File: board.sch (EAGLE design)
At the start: 31 parts, among them U3 STM32F405RG

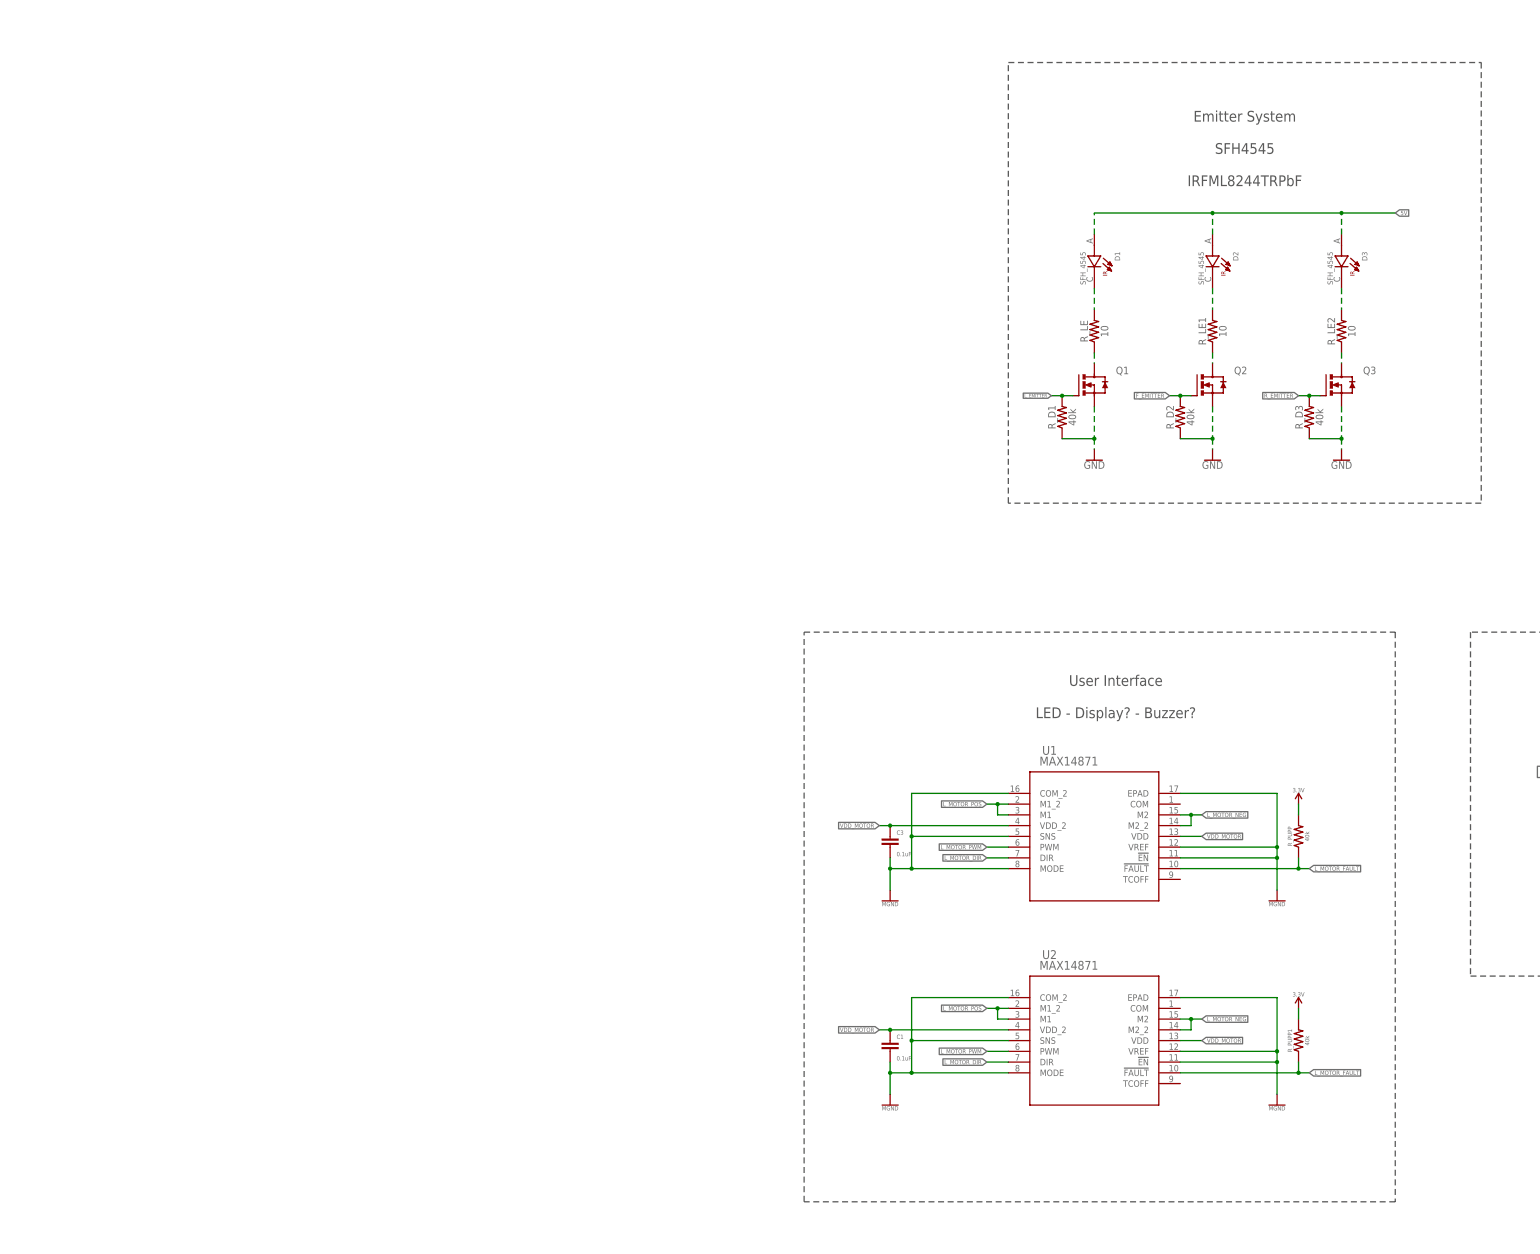
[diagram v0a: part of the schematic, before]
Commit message: Update Motor driver -> MAX14870
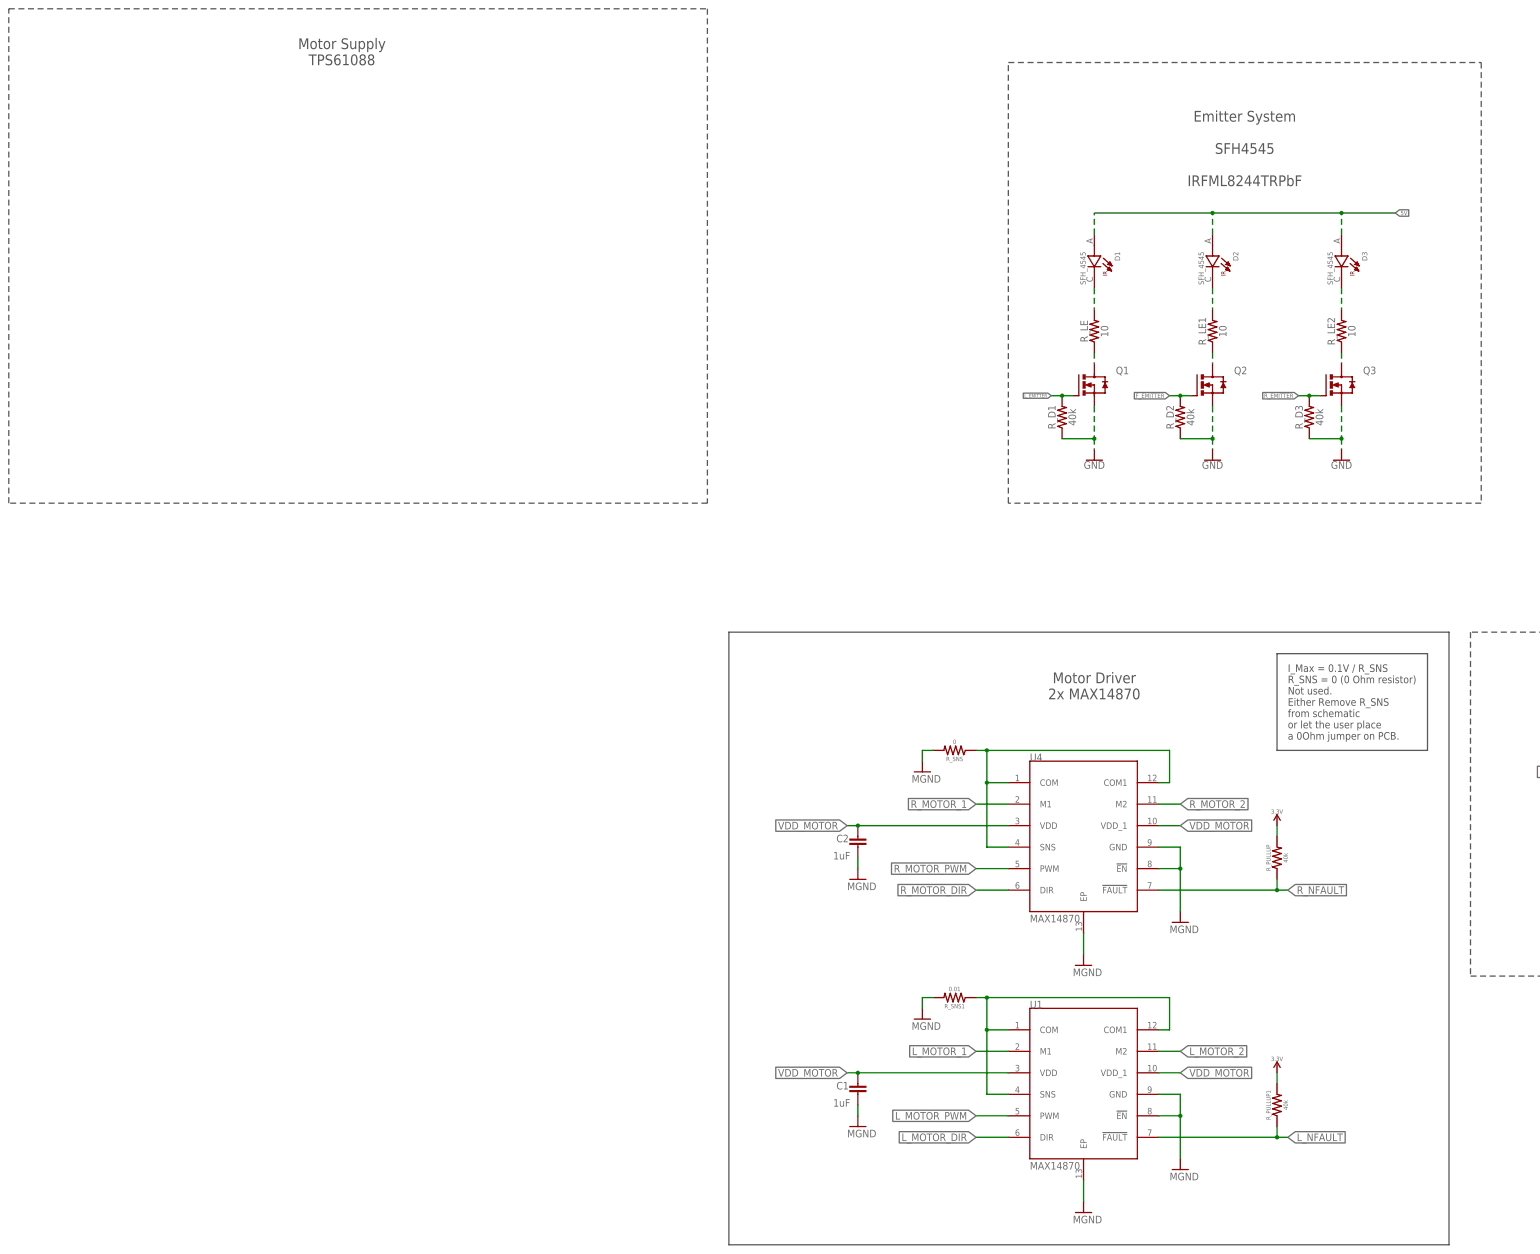
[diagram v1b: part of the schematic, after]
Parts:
- removed C3: 0.1uF, SparkFun-Capacitors:0.1UF-0603-25V-5%
- removed R_PUPP, R_PUPP1: 40k, SparkFun-Resistors:2.2KOHM-0603-1/10W-1%
- removed U2: (no value), Isaks Bibliotek:MAX14871EUE
- added C2: 1uF, Resistor_Capacitor:CC0603JRNPO9BN220
- added R_PULLUP, R_PULLUP1: 40k, SparkFun-Resistors:2.2KOHM-0603-1/10W-1%
- added R_SNS: 0, SparkFun-Resistors:2.2KOHM-0603-1/10W-1%
- added R_SNS1: 0.01, SparkFun-Resistors:2.2KOHM-0603-1/10W-1%
- added U4: MAX14870, Isaks Bibliotek:MAX14870
- C1: value 0.1uF -> 1uF; device SparkFun-Capacitors:0.1UF-0603-25V-5% -> Resistor_Capacitor:CC0603JRNPO9BN220
- U1: value (none) -> MAX14870; device Isaks Bibliotek:MAX14871EUE -> Isaks Bibliotek:MAX14870
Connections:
- removed net L_MOTOR_FAULT: R_PUPP.1, R_PUPP1.1, U1.!FAULT, U2.!FAULT
- removed net L_MOTOR_NEG: U1.M2, U1.M2_2, U2.M2, U2.M2_2
- removed net L_MOTOR_POS: U1.M1, U1.M1_2, U2.M1, U2.M1_2
- removed net MGND: C1.2, C3.2, U1.!EN, U1.COM_2, U1.EPAD, U1.MODE, U1.SNS, U1.VREF, U2.!EN, U2.COM_2, U2.EPAD, U2.MODE, U2.SNS, U2.VREF
- new net L_MOTOR_1: U1.M1
- new net L_MOTOR_2: U1.M2
- new net L_NFAULT: R_PULLUP1.1, U1.!FAULT
- new net N$10: R_SNS1.1, U1.COM, U1.COM1, U1.SNS
- new net N$12: R_SNS.1, U4.COM, U4.COM1, U4.SNS
- new net R_MOTOR_1: U4.M1
- new net R_MOTOR_2: U4.M2
- new net R_MOTOR_DIR: U4.DIR
- new net R_MOTOR_PWM: U4.PWM
- new net R_NFAULT: R_PULLUP.1, U4.!FAULT
- net 3.3V: now also R_PULLUP.2, R_PULLUP1.2; no longer R_PUPP.2, R_PUPP1.2
- net GND: now also C1.2, C2.2, R_SNS.2, R_SNS1.2, U1.!EN, U1.EP, U1.GND, U4.!EN, U4.EP, U4.GND
- net L_MOTOR_DIR: no longer U2.DIR
- net L_MOTOR_PWM: no longer U2.PWM
- net VDD_MOTOR: now also C2.1, U1.VDD_1, U4.VDD, U4.VDD_1; no longer C3.1, U1.VDD_2, U2.VDD, U2.VDD_2
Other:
- note added: "I_Max = 0.1V / R_SNS R_SNS = 0 (0 Ohm resistor) Not used. Either Remove R_SNS from schematic or let the user place a 0Ohm jumper on PCB."
- note added: "Motor Driver 2x MAX14870"
- note added: "Motor Supply TPS61088"
- moved on the sheet: C1

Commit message: 2V regulator + new motor driver
Changed motor driver from MAX14870 to TB6612FNG for easier soldering. Added a 2V switching DC regulator for more efficient emitter driving.
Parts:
- removed R_D1, R_D2, R_D3: 40k, SparkFun-Resistors:0.22OHM-0805-1/4W-1%
- removed R_LE, R_LE1, R_LE2: 10, SparkFun-Resistors:0.22OHM-0805-1/4W-1%
- removed R_PULLUP, R_PULLUP1: 40k, SparkFun-Resistors:2.2KOHM-0603-1/10W-1%
- removed R_SNS: 0, SparkFun-Resistors:2.2KOHM-0603-1/10W-1%
- removed R_SNS1: 0.01, SparkFun-Resistors:2.2KOHM-0603-1/10W-1%
- removed U4: MAX14870, Isaks Bibliotek:MAX14870
- added C3: 10u, CASE-RCL:KEMET_C
- added C_IN, C_OUT: 10u, CASE-RCL:C0805
- added C_VC: 470pF, CASE-RCL:C0603
- added IC1: LMZ10501SILT, Isaks Bibliotek:LMZ10501SILT
- added Q4: IRFML8244TRPBF, Isaks Bibliotek:IRFML8244TRPBF
- added R10, R11, R12: 10k, CASE-RCL:R0603
- added R13: 2.2k, CASE-RCL:R0603
- added R7, R8, R9: 0.75, CASE-RCL:R0603
- added RB: 150k, CASE-RCL:R0603
- added RT: 290k, CASE-RCL:R0603
- added U$4: SMT-0540-S-R, Isaks Bibliotek:SMT-0540-S-R
- added U$5: 1N4148WX_SOD-323-2, 1N4148WX_SOD-323-2:1N4148WX_SOD-323-2
- C1, C2: value 1uF -> 0.1u; device Resistor_Capacitor:CC0603JRNPO9BN220 -> CASE-RCL:C0603
- LED_B, LED_G, LED_R: value HSMH-C190 -> CHIP-LED0603; device LED:HSMH-C190 -> CASE-LED:CHIP-LED0603
- Q1, Q2, Q3: value (none) -> IRFML8244TRPBF; device MOSFET N-Channel SOT23:MOSFET_N_SOT231 -> Isaks Bibliotek:IRFML8244TRPBF
- R1, R2: device SparkFun-Resistors:2.2KOHM-0603-1/10W-1% -> CASE-RCL:R0603
- R3: value 2.2k -> 10k; device SparkFun-Resistors:2.2KOHM-0603-1/10W-1% -> CASE-RCL:R0603
- U1: value MAX14870 -> TB6612FNG; device Isaks Bibliotek:MAX14870 -> Isaks Bibliotek:TB6612FNG
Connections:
- removed net AGND: R1.1, R2.1, R3.1
- removed net L_MOTOR_1: U1.M1
- removed net L_MOTOR_2: U1.M2
- removed net L_MOTOR_DIR: U1.DIR
- removed net L_MOTOR_PWM: U1.PWM
- removed net L_NFAULT: R_PULLUP1.1, U1.!FAULT
- removed net N$12: R_SNS.1, U4.COM, U4.COM1, U4.SNS
- removed net R_MOTOR_1: U4.M1
- removed net R_MOTOR_2: U4.M2
- removed net R_MOTOR_DIR: U4.DIR
- removed net R_MOTOR_PWM: U4.PWM
- removed net R_NFAULT: R_PULLUP.1, U4.!FAULT
- removed net VDD_MOTOR: C1.1, C2.1, U1.VDD, U1.VDD_1, U4.VDD, U4.VDD_1
- new net 2V: C_OUT.1, D1.A, D2.A, D3.A, IC1.FB, IC1.VOUT
- new net BUZZER: Q3.G, R3.2
- new net ML_IN1: U1.BIN1
- new net ML_IN2: U1.BIN2
- new net MOTOR_L_1: U1.M_B1@1, U1.M_B1@2
- new net MOTOR_L_2: U1.M_B2@1, U1.M_B2@2
- new net MOTOR_R_1: U1.M_A1@1, U1.M_A1@2
- new net MOTOR_R_2: U1.M_A2@1, U1.M_A2@2
- new net MR_IN1: U1.AIN1
- new net MR_IN2: U1.AIN2
- new net N$11: C_VC.1, IC1.VCON, RB.2, RT.1
- new net N$13: Q3.D, U$4.-, U$5.+
- new net PWM_L: U1.PWMB
- new net PWM_R: U1.PWMA
- new net VIN: C2.1, C3.+
- new net VM: U1.VM@1, U1.VM@2, U1.VM@3
- net 3.3V: now also C1.1, U$4.+, U$5.-, U1.STBY, U1.VCC; no longer R_PULLUP.2, R_PULLUP1.2
- net 5V: now also C_IN.1, IC1.VIN; no longer D1.A, D2.A, D3.A
- net F_EMITTER: now also Q1.G, R10.2; no longer Q2.G, R_D2.2
- net GND: now also C3.-, C_IN.2, C_OUT.2, C_VC.2, IC1.EP, IC1.PGND, IC1.SGND, Q4.S, R1.1, R10.1, R11.1, R12.1, R13.1, R2.1, R3.1, RB.1, U1.M_GND1@1, U1.M_GND1@2, U1.M_GND2@1, U1.M_GND2@2; no longer R_D1.1, R_D2.1, R_D3.1, R_SNS.2, R_SNS1.2, U1.!EN, U1.EP, U4.!EN, U4.EP, U4.GND
- net L_EMITTER: now also Q4.G, R11.2; no longer Q1.G, R_D1.2
- net L_SENSE: now also R13.2; no longer R1.2
- net M_SENSE: now also R1.2; no longer R2.2
- net N$1: now also Q4.D, R7.1; no longer Q1.D, R_LE.1
- net N$10: now also IC1.VREF, RT.2; no longer R_SNS1.1, U1.COM, U1.COM1, U1.SNS
- net N$2: now also R7.2; no longer R_LE.2
- net N$3: now also LED_R.K; no longer LED_R.C
- net N$4: now also Q1.D, R8.1; no longer Q2.D, R_LE1.1
- net N$5: now also R8.2; no longer R_LE1.2
- net N$6: now also LED_G.K; no longer LED_G.C
- net N$7: now also Q2.D, R9.1; no longer Q3.D, R_LE2.1
- net N$8: now also R9.2; no longer R_LE2.2
- net N$9: now also LED_B.K; no longer LED_B.C
- net R_EMITTER: now also Q2.G, R12.2; no longer Q3.G, R_D3.2
- net R_SENSE: now also R2.2; no longer R3.2
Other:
- note added: "2V Regulator"
- note added: "3.3V output from MCU I = (3.3-2)/1k = 18mA"
- note added: "C_IN, C_OUT, C_VC >= 6.3V, X7R or X5R"
- note added: "Emitter System"
- note added: "Motor Driver TB6612FND Dual"
- note added: "RB = (VOUT / (5.875 - VOUT) * RT 80K <= RT <= 300K For fixed VOUT = 2V: RB = RT * 0.516129 ex. RT = 290k => RB = 150K"
- note added: "STBY should perhaps be controller by MCU"
- note added: "User Interface LED + Buzzer + Display?"
- note added: "V_in = 2 V I = 333 mAh V_f = 1.75 V R = (VIN - 1.75) / 0.333 = = 0.75 P_rloss = 0.75*0.333^2 = = 80 mW"
- note removed: "Emitter System SFH4545 IRFML8244TRPbF"
- note removed: "I_Max = 0.1V / R_SNS R_SNS = 0 (0 Ohm resistor) Not used. Either Remove R_SNS from schematic or let the user place a 0Ohm jumper on PCB."
- note removed: "Motor Driver 2x MAX14870"
- note removed: "User Interface LED - Display? - Buzzer?"
- moved on the sheet: C1, C2

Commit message: Power Regulators + Created board file
Alot has been done in this update.
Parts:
- removed U$2, U$3: TEFT4300, Isaks Bibliotek:TEFT4300"
- removed U$5: 1N4148WX_SOD-323-2, 1N4148WX_SOD-323-2:1N4148WX_SOD-323-2
- added C10, C12, C14, C18, C28, C4, C6, C8: 0.1u, CASE-RCL:C0603
- added C11, C13, C5, C7, C9: 10u, CASE-RCL:C0603
- added C15, C29: 2.2u, CASE-RCL:C0603
- added C16: 0.1u, CASE-RCL:C0805
- added C17, C19, C20, C22, C25, C32, C33: 22u, CASE-RCL:C0805
- added C21: 27p, CASE-RCL:C0603
- added C23: 560p, CASE-RCL:C0603
- added C24: 1u, CASE-RCL:C0805
- added C26, C27: 10u, Isaks Bibliotek:SMC_A
- added C31: 3300p, CASE-RCL:C0603
- added D4, D5, D6, D8: TEFT4300, Isaks Bibliotek:TEFT4300
- added D7: SFH_4545, Isaks Bibliotek:SFH_4545
- added FP1: 10u, CASE-RCL:WE-CBF_0805
- added IC2: TPS61088RHLR, Isaks Bibliotek:TPS61088RHLR
- added L1: 2.2u, Isaks Bibliotek:XAL5030-222MEC
- added Q5: IRFML8244TRPBF, Isaks Bibliotek:IRFML8244TRPBF
- added R14: 1k, CASE-RCL:R0603
- added R15, R23: 10k, CASE-RCL:R0603
- added R16: 1.8k, CASE-RCL:R0603
- added R17: 150k, CASE-RCL:R0603
- added R18: 180k, CASE-RCL:R0603
- added R19, R_FBB: 20k, CASE-RCL:R0603
- added R20: 30k, CASE-RCL:R0603
- added R21: 112k, CASE-RCL:R0603
- added R_FBT: 105k, CASE-RCL:R0603
- added S1: LMZ21701, Isaks Bibliotek:LMZ21701
- added VR1: LM1117-3.3, Isaks Bibliotek:LM1117-3.3
- D1, D2, D3: device SFH_4545:SFH_4545 -> Isaks Bibliotek:SFH_4545
- R1, R13, R2: value 2.2k -> 1.8k
- R12: value 10k -> 0.75
- R4, R5: device Resistor_Capacitor:RC0603JR-070RL -> CASE-RCL:R0603
- R6: value 1k -> 0.75; device Resistor_Capacitor:RC0603JR-070RL -> CASE-RCL:R0603
- R8: value 0.75 -> 10k
- U$1: value TEFT4300 -> 1N4148WX; device Isaks Bibliotek:TEFT4300" -> Isaks Bibliotek:DIODE_1N4148WX
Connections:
- removed net F_EMITTER: Q1.G, R10.2
- removed net L_SENSE: R13.2, U$1.CATHODE_OUT
- removed net M_SENSE: R1.2, U$2.CATHODE_OUT
- removed net N$8 (its old number): D3.C, R9.2
- removed net R_SENSE: R2.2, U$3.CATHODE_OUT
- removed net VIN: C2.1, C3.+
- removed net VM: U1.VM@1, U1.VM@2, U1.VM@3
- new net 12V: C19.1, C2.1, C20.1, C22.1, C24.1, C3.+, IC2.VOUT@1, IC2.VOUT@2, IC2.VOUT@3, R18.1, U1.VM@1, U1.VM@2, U1.VM@3
- new net 3.3VA: C28.1, C29.1, D4.C_+, D5.C_+, D6.C_+, D8.C_+, FP1.2
- new net FL_EMITTER: Q1.G, R8.2
- new net FL_RECEIVER: D5.E_-, R1.2
- new net FR_EMITTER: Q2.G, R10.2
- new net FR_RECEIVER: D8.E_-, R16.2
- new net GND_A: C28.2, C29.2, R1.1, R13.1, R16.1, R2.1
- new net GND_M: C1.2, C2.2, C3.-, U1.GND, U1.M_GND1@1, U1.M_GND1@2, U1.M_GND2@1, U1.M_GND2@2
- new net GND_SW: C15.2, C16.2, C17.2, C18.2, C19.2, C20.2, C21.2, C22.2, C23.2, C24.2, C25.2, IC2.AGND, IC2.MODE, IC2.NC@1, IC2.NC@2, IC2.PGND, R19.2, R21.2
- new net L_RECEIVER: D4.E_-, R13.2
- new net N$12: D7.-_CATHODE, R12.2
- new net N$14: D3.-_CATHODE, R9.2
- new net N$15: C14.1, IC2.SW@1, IC2.SW@2, IC2.SW@3, IC2.SW@4, L1.2, R17.1
- new net N$16: IC2.FSW, R17.2
- new net N$17: C14.2, IC2.BOOT
- new net N$18: C15.1, IC2.EN, IC2.VCC
- new net N$19: C18.1, IC2.SS
- new net N$20: IC2.FB, R18.2, R19.1
- new net N$21: C21.1, IC2.COMP, R20.1
- new net N$22: IC2.ILIM, R21.1
- new net N$23: C23.1, R20.2
- new net N$24: C31.1, S1.SS
- new net N$25: R_FBB.2, R_FBT.2, S1.FB
- new net N$26: C33.2, R_FBB.1
- new net N$27: R23.1, S1.PG
- new net N$7: Q5.D, R12.1
- new net R_RECEIVER: D6.E_-, R2.2
- new net V_BAT: C16.1, C17.1, C25.1, C32.1, IC2.VIN, L1.1, S1.VIN
- net 2V: now also C10.1, C11.1, C12.1, C13.1, C6.1, C7.1, C8.1, C9.1, D1.+_ANODE, D2.+_ANODE, D3.+_ANODE, D7.+_ANODE; no longer D1.A, D2.A, D3.A
- net 3.3V: now also C27.+, C4.1, C5.1, FP1.1, U$1.+_ANODE, VR1.VOUT; no longer U$1.ANODE_IN, U$2.ANODE_IN, U$3.ANODE_IN, U$5.-
- net 5V: now also C26.+, C33.1, R23.2, R_FBT.1, S1.VOS, S1.VOUT, VR1.VIN
- net GND: now also C10.2, C11.2, C12.2, C13.2, C26.-, C27.-, C31.2, C32.2, C4.2, C5.2, C6.2, C7.2, C8.2, C9.2, Q5.S, R14.1, R15.1, R8.1, S1.GND@1, S1.GND@2, S1.GND@3, VR1.GND; no longer C1.2, C2.2, C3.-, R1.1, R12.1, R13.1, R2.1, R6.1, U1.GND, U1.M_GND1@1, U1.M_GND1@2, U1.M_GND2@1, U1.M_GND2@2
- net N$13: now also U$1.-_CATHODE; no longer U$5.+
- net N$2: now also D1.-_CATHODE; no longer D1.C
- net N$3: now also R14.2; no longer R4.2
- net N$4: now also R6.1; no longer R8.1
- net N$5: now also D2.-_CATHODE, R6.2; no longer D2.C, R8.2
- net N$6: now also R4.2; no longer R5.2
- net N$9: now also R5.2; no longer R6.2
- net R_EMITTER: now also Q5.G, R15.2; no longer Q2.G, R12.2
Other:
- note added: "3.3 V & 3.3VA Regulator (LDO)"
- note added: "3.3V output from MCU Could be improved with mosfets driving I = (3.3-2)/1k = 18mA => ~60mA output from MCU"
- note added: "5V Regulator"
- note added: "Cin and Cout: >= 10u Tantalum Inductor (0603 ferrite bead): 10u to act as a LC filter"
- note added: "Emitter System SFH4545"
- note added: "Motor Supply TPS61088 - 12V"
- note added: "Output Voltage: Rfbt = Rfbb * (Vout/0.8 - 1) Rfbb < 400k Rfbb = 20k => Rfbt = 105k Ifb = 5 / (105+20) = 60 uA (2 uA min) PG (power good): Datasheet => 10k SS (soft start): Datasheet => 3300pF Vin Caps: Low ESR multilayer ceramic >= 10u >= 0805 >= 20V X5R or X7R Vout Caps: >= 10u >= 0805 >= 10V X5R or X7R"
- note added: "PWM Mode => Vref = 1.204 V Switching Frequency: 1 MHz => ~150 kΩ Voltage output: R2 = 20k R1 = (V_out - Vref) * R2 / Vref = 180k i = 12 V / 200k = 60uA (good) Startup Time: t = Vref * Css / Iss = 1.204*0.1u/5u = 2 mS Inductor (2.2uH XAL5030-222): Idc = Vout*Iout/(Vin*efficiency) = 4.7A Iripp = 1.36A (1MHz) Iripp = 8.5A (200kHz) I_Lpeak = 5.3 / 9 A Inductor sat current = 9A Current Limiting: I_lim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"
- note removed: "3.3V output from MCU I = (3.3-2)/1k = 18mA"
- note removed: "Emitter System"
- note removed: "Motor Supply TPS61088"
- moved on the sheet: C1, C2, C3, C_IN, C_OUT, C_VC, IC1, LED_B, LED_G, LED_R, Q1, Q2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

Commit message: Voltmeter Monitors on Boost, Batt, Cell1 and 5V Power LED
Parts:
- added 5V_PWR: CHIP-LED0603, CASE-LED:CHIP-LED0603
- added C30, C35: 0.1u, CASE-RCL:C0603
- added C34: 10n, CASE-RCL:C0603
- added R22: 47k, CASE-RCL:R0603
- added R24, R27, R31: 10k, CASE-RCL:R0603
- added R25: 1k, CASE-RCL:R0603
- added R26, R28: 20k, CASE-RCL:R0603
- added R29, R30, R_MOSI, R_SCL, R_SCLK, R_SDA: 0, CASE-RCL:R0603
- added SW: SPDT-500SSP1S1M6QEA, Isaks Bibliotek:SPDT-500SSP1S1M6QEA
- added U$6, U$7: SPLITTER, Isaks Bibliotek:SPLITTER
- added U2: MPU6500, Isaks Bibliotek:MPU6500
- added X1: JST-XH, JST XH Connectors:JST-XH-03-PIN-LONG-PAD
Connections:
- new net !CS: R30.1
- new net INT: U2.INT
- new net MISO: U2.AD0/MISO
- new net MOSI: R_MOSI.1
- new net N$28: C30.1, U2.REGOUT
- new net N$29: R_MOSI.2, R_SDA.2, U2.SDA/MOSI
- new net N$30: R_SCL.2, R_SCLK.2, U2.SCL/SCLK
- new net N$31: 5V_PWR.K, R25.2
- new net N$33: R26.2, X1-2.S
- new net N$36: R29.2, R30.2, U2.!CS
- new net N$38: R28.2, SW.3, SW.COM, X1-3.S
- new net SCL: R_SCL.1
- new net SCLK: R_SCLK.1
- new net SDA: R_SDA.1
- new net VOLM_BATT: R28.1, R31.2
- new net VOLM_CELL1: R26.1, R27.2
- new net VOLTM_BOOST: R22.1, R24.2
- net 12V: now also R22.2
- net 3.3VA: now also C34.1, C35.1, R29.1, U2.VDD, U2.VDDIO
- net 5V: now also 5V_PWR.A
- net GND: now also R27.1, R31.1, U$6.2, U$7.2, X1-1.S
- net GND_A: now also C30.2, C34.2, C35.2, U2.FSYNC, U2.GND, U2.RESV
- net GND_M: now also U$6.1
- net GND_SW: now also R24.1, U$7.1
- net N$26: now also R25.1
- net V_BAT: now also SW.1
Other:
- note added: "Battery Connector"
- note added: "Gyro MPU6050"
- note added: "Most MPU6050/6500 libraries use I2C but SPI is faster/better? there is confiburable 0 ohm resistors to choose which interface to use."
- note added: "Voltage Divider: R1 = 20k R2 = 10k Voltmeter Cell1: [3, 4.2] V => [1, 1.4] V Voltmeter Entire Battery: [6, 8.4] V => [2, 2.8] V"
- moved on the sheet: C31, C32, C33, R23, R_FBB, R_FBT, S1
